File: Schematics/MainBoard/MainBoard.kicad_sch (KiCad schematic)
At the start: 48 parts, among them J1 USB_C_Receptacle_USB2.0, Q1 DTC114T, Q2 DTC114T, SW2 PROG, SW3 RESET, U1 CP2102N-A01-GQFN28, U2 ESP32-S2-WROVER, U3 TPS63001, U4 MCP73831-2-OT

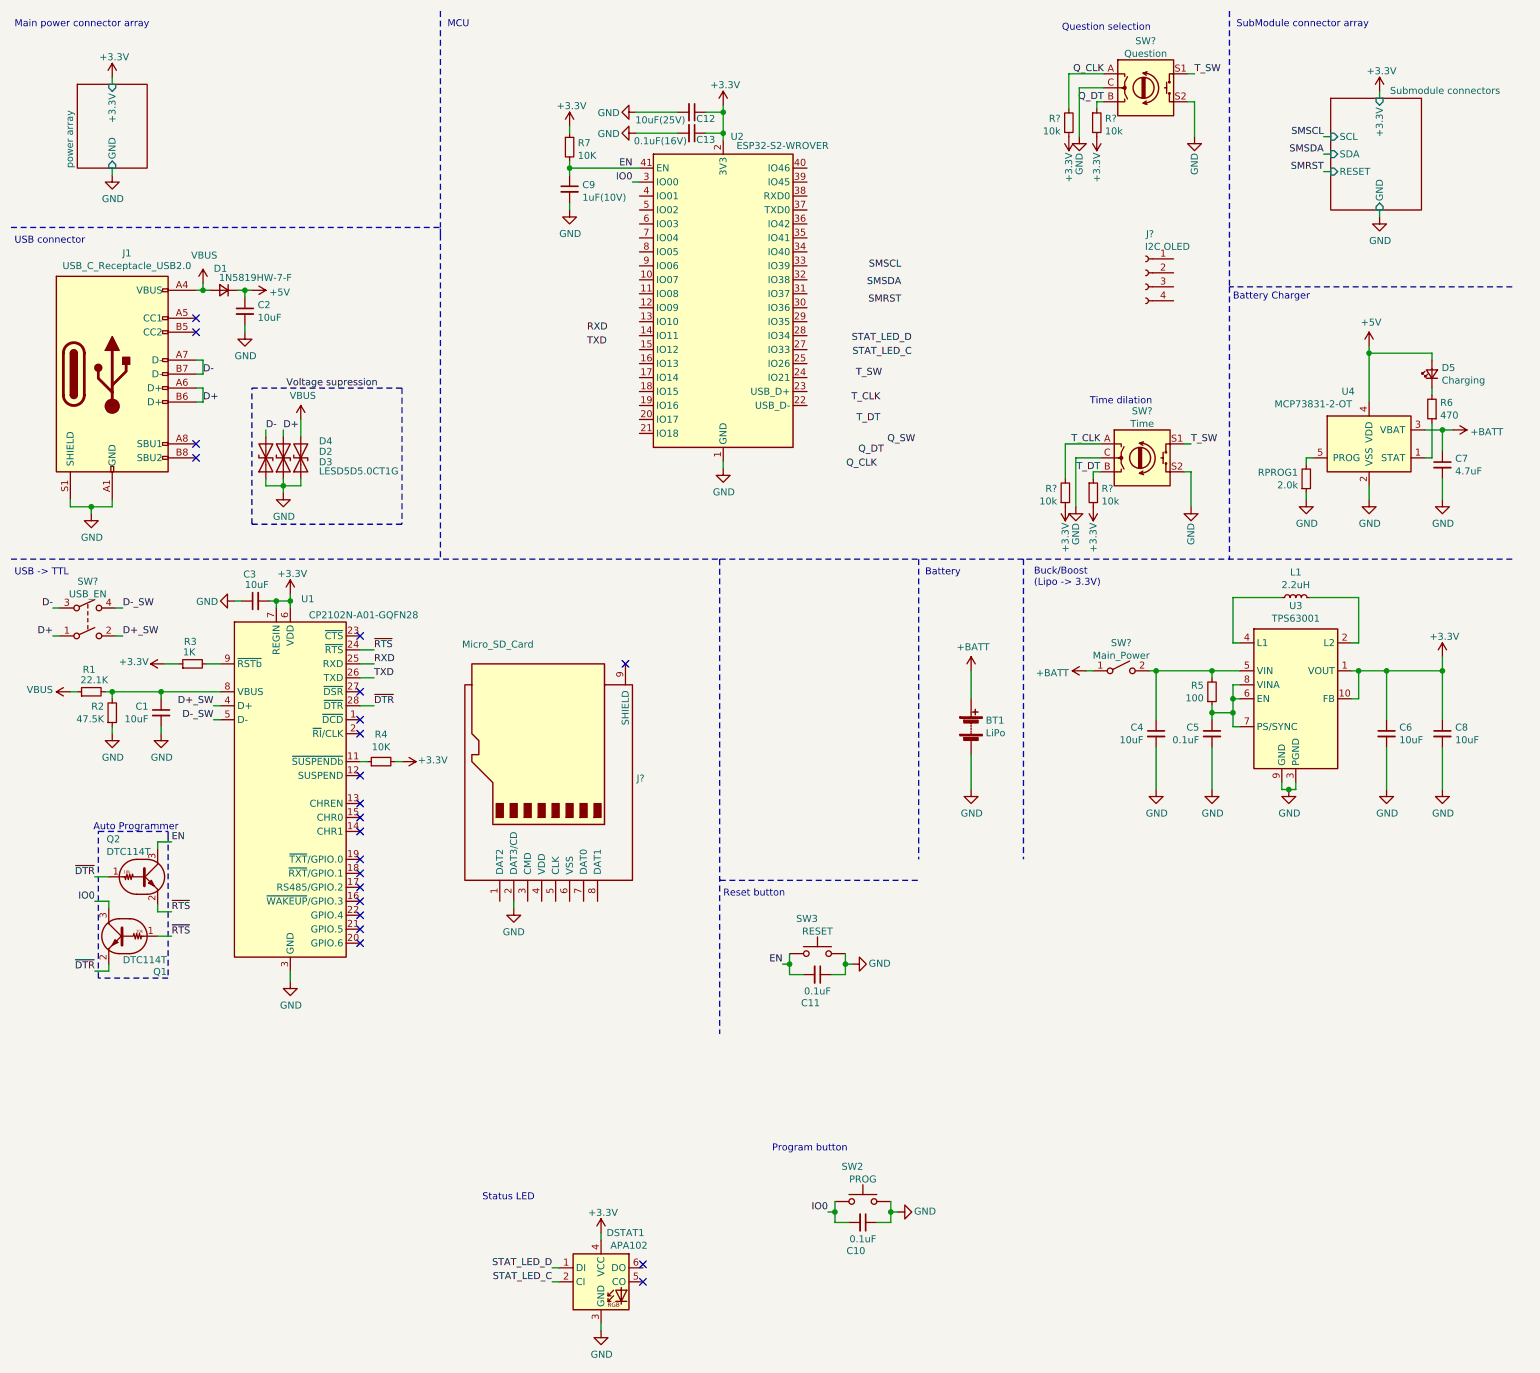
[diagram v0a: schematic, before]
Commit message: Finished circuit - pre mousebites
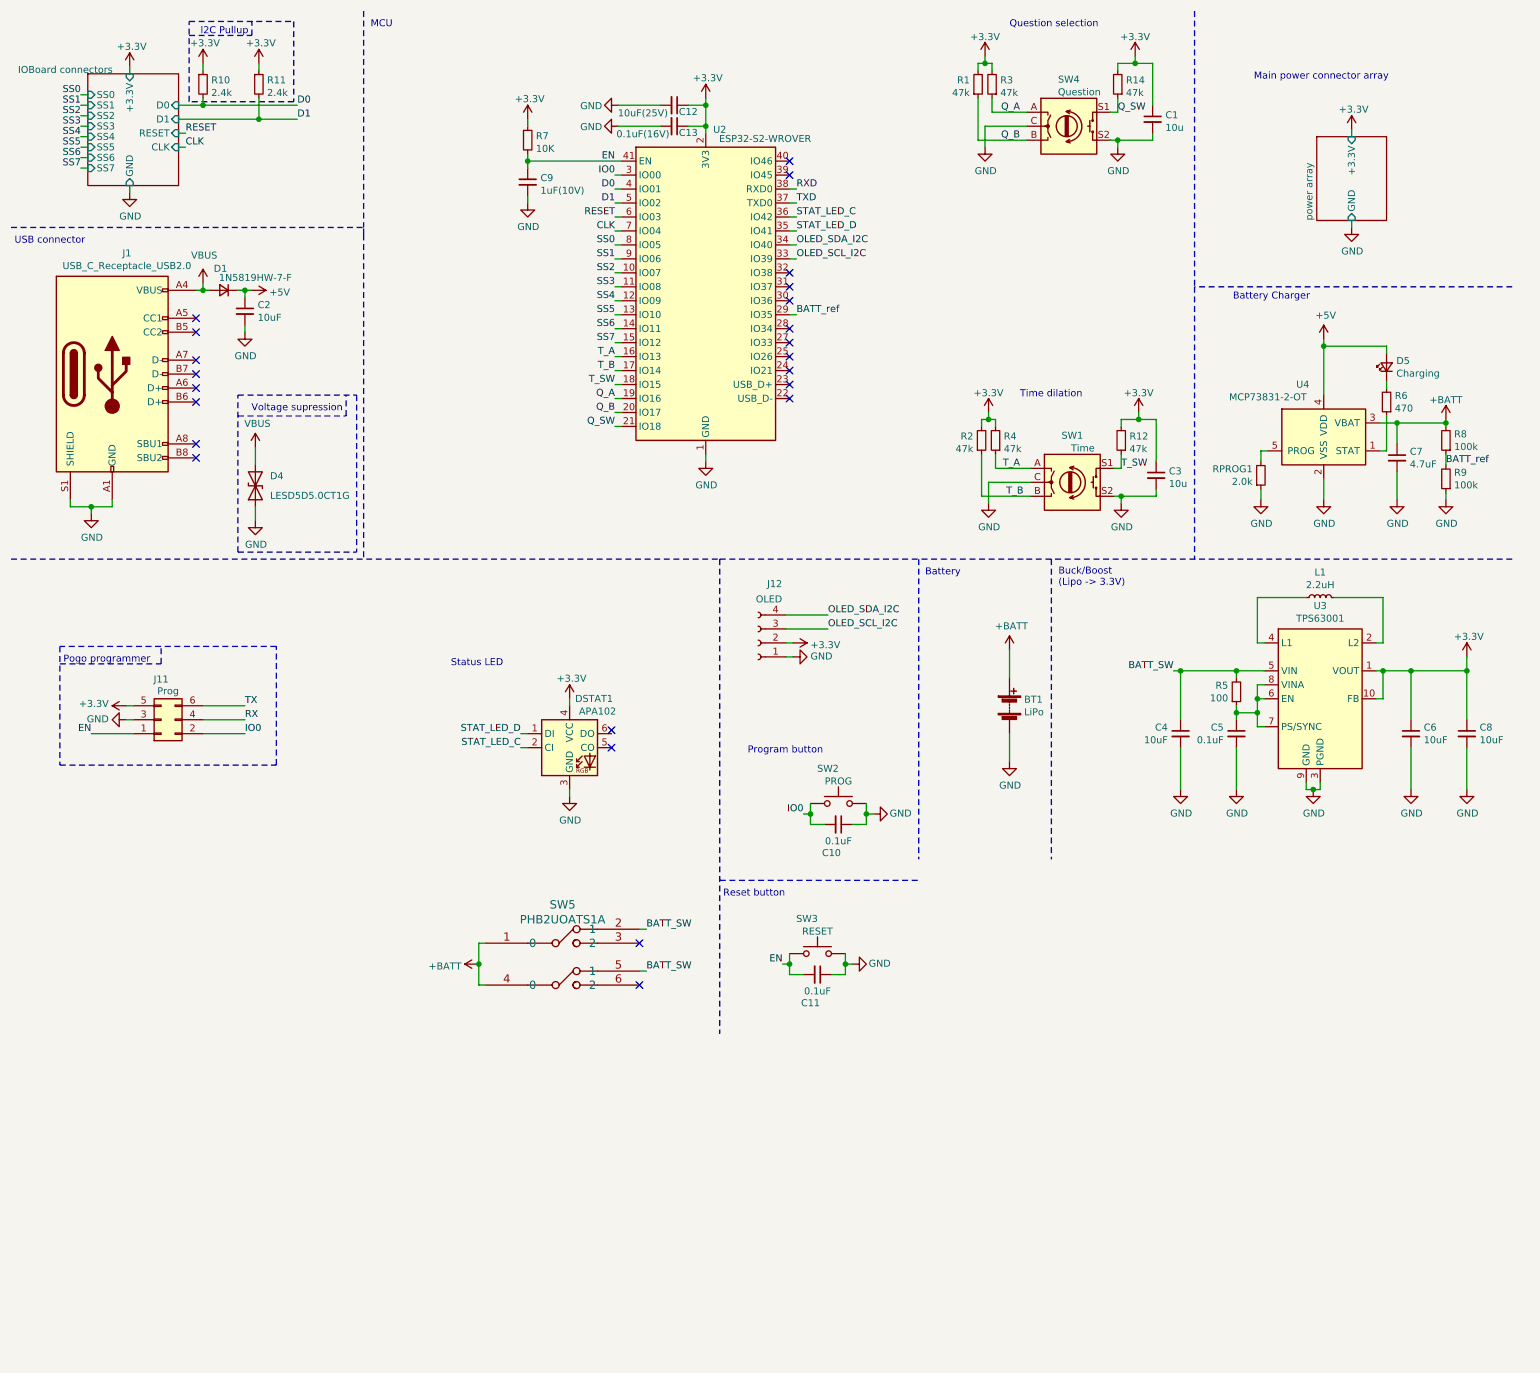
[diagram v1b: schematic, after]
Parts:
- removed D2, D3: LESD5D5.0CT1G, Diode_SMD:D_SOD-523, symbol Device:D_TVS
- removed J?: I2C OLED, symbol Connector:Conn_01x04_Female
- removed J?: Micro_SD_Card, symbol Connector:Micro_SD_Card
- removed Q1, Q2: DTC114T, libs:SOT346, symbol Transistor_BJT:DTC114T
- removed R? (x4): 10k, symbol Device:R_Small
- removed SW?: USB_EN, symbol Switch:SW_DPST
- removed SW?: Main_Power, symbol Switch:SW_SPST
- removed SW?: Time, symbol Device:Rotary_Encoder_Switch
- removed SW?: Question, symbol Device:Rotary_Encoder_Switch
- removed U1: CP2102N-A01-GQFN28, Package_DFN_QFN:QFN-28-1EP_5x5mm_P0.5mm_EP3.35x3.35mm, symbol Interface_USB:CP2102N-A01-GQFN28
- added J11: Prog, Connector:Tag-Connect_TC2030-IDC-NL_2x03_P1.27mm_Vertical, symbol Connector_Generic:Conn_02x03_Odd_Even
- added J12: OLED, Connector_PinHeader_2.00mm:PinHeader_1x04_P2.00mm_Vertical_SMD_Pin1Left, symbol Connector:Conn_01x04_Female
- added R10, R11: 2.4k, Resistor_SMD:R_0603_1608Metric, symbol Device:R_Small
- added R12, R14: 47k, Resistor_SMD:R_0603_1608Metric, symbol Device:R_Small
- added R8, R9: 100k, Resistor_SMD:R_0603_1608Metric, symbol Device:R_Small
- added SW1: Time, Rotary_Encoder:RotaryEncoder_Alps_EC11E-Switch_Vertical_H20mm, symbol Device:Rotary_Encoder_Switch
- added SW4: Question, Rotary_Encoder:RotaryEncoder_Alps_EC11E-Switch_Vertical_H20mm, symbol Device:Rotary_Encoder_Switch
- added SW5: PHB2UOATS1A, PHB2UOATS1A:PHB2UOATS1A, symbol PHB2UOATS1A:PHB2UOATS1A
- C1, C3: value 10uF -> 10u
- R1: value 22.1K -> 47k
- R2: value 47.5K -> 47k
- R3: value 1K -> 47k
- R4: value 10K -> 47k
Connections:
- net +3V3: now also C1.1, C3.1, R1.2, R2.2, R3.2, J11.5 (Pin_5), J12.2 (Pin_2), R10.1, R11.1, R12.2, R14.2; no longer C3.2, R3.1
- net +BATT: now also R8.2, SW5.1 (0), SW5.4 (0)
- net EN: now also J11.1 (Pin_1)
- net GND: now also C3.2, J11.3 (Pin_3), J12.1 (Pin_1), R9.1, SW1.C, SW1.S2, SW4.C, SW4.S2; no longer C3.1, R2.1
- net IO0: now also J11.2 (Pin_2)
- net Q_SW: now also U2.21 (IO18), R14.1, SW4.S1
- net RXD: now also U2.38 (RXD0)
- net STAT_LED_C: now also U2.36 (IO42)
- net STAT_LED_D: now also U2.35 (IO41)
- net TXD: now also U2.37 (TXD0)
- net T_SW: now also U2.18 (IO15), R12.1, SW1.S1
- net VBUS: no longer R1.1
- net SS2: now reaches U2.10 (IO07)
- net SS3: now reaches U2.11 (IO08)
- net SS4: now reaches U2.12 (IO09)
- net SS5: now reaches U2.13 (IO10)
- net SS6: now reaches U2.14 (IO11)
- net SS7: now reaches U2.15 (IO12)
- net T_A: now reaches U2.16 (IO13)
- net T_A: now also R4.1, SW1.A
- net T_B: now reaches U2.17 (IO14)
- net T_B: now also R2.1, SW1.B
- net Q_A: now reaches U2.19 (IO16)
- net Q_A: now also R3.1, SW4.A
- net Q_B: now reaches U2.20 (IO17)
- net Q_B: now also R1.1, SW4.B
- net BATT_ref: now reaches U2.29 (IO35)
- net BATT_ref: now also R8.1, R9.2
- net OLED_SCL_I2C: now reaches U2.33 (IO39)
- net OLED_SCL_I2C: now also J12.3 (Pin_3)
- net OLED_SDA_I2C: now reaches U2.34 (IO40)
- net OLED_SDA_I2C: now also J12.4 (Pin_4)
- net D0: now reaches U2.4 (IO01)
- net D0: now also R10.2
- net D1: now reaches U2.5 (IO02)
- net D1: now also R11.2
- net RESET: now reaches U2.6 (IO03)
- net CLK: now reaches U2.7 (IO04)
- net SS0: now reaches U2.8 (IO05)
- net SS1: now reaches U2.9 (IO06)
- net BATT_SW: now reaches C4.1, R5.2, U3.5 (VIN)
- net BATT_SW: now also SW5.2 (1), SW5.5 (1)
- net D+: no longer names the net of J1.A6 (D+)
- net D+: no longer J1.B6 (D+)
- net D-: no longer names the net of J1.A7 (D-)
- net D-: no longer J1.B7 (D-)
- new net RX: J11.4 (Pin_4)
- new net TX: J11.6 (Pin_6)
- no-connect marks 22 -> 23
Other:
- sheet Submodule connectors renamed IOBoard connectors
- sheet IOBoard connectors: file submoduleConnectors.kicad_sch -> IOBoardConnectors.kicad_sch
- sheet IOBoard connectors ports: added CLK, D0, D1, SS0, SS1, SS2, SS3, SS4, SS5, SS6, SS7; removed SCL, SDA
- note added: "I2C Pullup"
- note added: "Pogo programmer"
- note added: "Voltage supression"
- note removed: "Auto Programmer"
- note removed: "SubModule connector array"
- note removed: "USB -> TTL"
- moved on the sheet: BT1, C10, C12, C13, C4, C5, C6, C7, C8, C9, D4, D5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
